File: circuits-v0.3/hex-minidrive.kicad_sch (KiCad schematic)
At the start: 97 parts, among them X1 16MHz

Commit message: Sketch out v0.3 of the servo driver, without the USB port.
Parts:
- removed D1: ~, Library:SOD-123_L2.7-W1.6-LS3.7-RD-1, symbol Library:B5819W_C8598 Schottky diode
- removed D2: ~, Library:SOT-23-3_L3.0-W1.7-P0.95-LS2.9-BR, symbol Library:PSM712-LF-T7 ETV/ESD Diodes
- removed H2: 2P-2.54mm-header, Library:HDR-TH_2P-P2.54-V-M, symbol Library:PZ254V-11-02P Connector 2P 2.54mm spacing
- removed H3: 10P 1.27mm header, Library:HDR-TH_HX-PZ1.27-1X10P-ZZ, symbol Library:HX PZ1.27-1X10P ZZ Connectors 10P 1.27mm header
- removed L3: 300mΩ, Library:L0805, symbol Library:GZ2012D601TF Ferrite bead
- removed R11, R12: 5.1kΩ, Library:R0603, symbol Library:0603WAF5101T5E Resistor 5.1kΩ
- removed USB1: ~, Library:USB-C-SMD_TYPE-C16PIN, symbol Library:TYPE-C16PIN USB connector
- renumbered FPC4 to FPC1
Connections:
- no-connect marks 21 -> 17
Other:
- note removed: "Elestrostatic discharge protection"
- note removed: "Eusebiu - USB C"
- note removed: "Ferrite bead filtering 5V USB line."
- note removed: "Note: pullup resistor is included in STM32G4 series."
- note removed: "SBU1 and SBU2 are coonected to Reset and Boot0 pins so we can flash new software over USB with the builtin bootloader, let's see if it works."
- company: (none) -> Hex Robotics Limited
- title: (none) -> Hex mini servo driver
- moved on the sheet: FPC1
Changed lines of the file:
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@@
 	(generator_version "9.0")
 	(paper "A2")
+	(title_block
+		(title "Hex mini servo driver")
+		(rev "version 0.3")
+		(company "Hex Robotics Limited")
+		(comment 1 "Author: Calin Mocanu")
+	)

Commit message: Think about v0.3 driver circuit.
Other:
- note added: "Hex Mini Driver This is a quad output, motor driver for stepper, brushless or 2 DC motors. The board comes provisioned with 2 I2C connectors for plug in rotation sensors AS5600 (preferably the Hex mini flex rotation sensor). Target limits are 6-30V supply range and 5A of current. TODO for this version: [ ] Swap components to 0402 where possible, 0603 where not. [ ] Optimize for 2 sided tiny circu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"
- note removed: "Hex Mini Driver This is a quad output, motor driver for stepper, brushless or 2 DC motors. The board comes provisioned with 2 I2C connectors for plug in rotation sensors AS5600 (preferably the Hex mini flex rotation sensor). Target limits are 6-30V supply range and 5A of current."

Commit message: Start re-wiring v0.3 motor driver, 16mm width is too tight.
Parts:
- removed C101, C201, C30, C301, C401: 1nF, Library:C0603, symbol Library:CL10B102KB8NNNC Capacitor 1nF
- removed C12, C7, C8, C803: 1uF, Library:C0603, symbol Library:CL10A105KB8NNNC Capacitor 1uF
- removed C13, C24, C25, C26, C27, C801, C802: 100nF, Library:C0603, symbol Library:CC0603KRX7R9BB104 Capacitor 100nF
- removed C20, C21: 15pF, Library:C0603, symbol Library:CL10C150JB8NNNC Capacitor 15pF
- removed C34, C9: 10nF, Library:C0603, symbol Library:0603B103K500NT Capacitor 10nF
- removed C6: 100pF, Library:C0603, symbol Library:CL10C101JB8NNNC Capacitor 100pF
- removed R10: 49.9Ω, Library:R0603, symbol Library:0603WAF499JT5E Resistor 49.9Ω
- removed R101, R102, R201, R202, R301, R302, R401, R402: 10Ω, Library:R0603, symbol Library:0603WAF100JT5E Resistor 10Ω
- removed R103, R17, R203, R303, R403, R5: 100kΩ, Library:R0603, symbol Library:0603WAF1003T5E Resistor 100kΩ
- removed R104, R204, R304, R404: 5.1kΩ, Library:R0603, symbol Library:0603WAF5101T5E Resistor 5.1kΩ
- removed R18, R801, R802: 10kΩ, Library:R0603, symbol Library:0603WAF1002T5E Resistor 10kΩ
- removed R21, R22, R23: 1.5kΩ, Library:R0603, symbol Library:0603WAF1501T5E Resistor 1.5kΩ
- removed R6: 13kΩ, Library:R0603, symbol Library:0603WAF1302T5E Resistor 13kΩ
- added C101, C106, C108, C109, C110, C111, C112, C113, C114, C21: 100nF, Library:C0402, symbol Library:CL05B104KB54PNC Capacitor 100nF 50V
- added C102, C105, C107, C31, C32: 1uF, Library:C0402, symbol Library:CL05A105KA5NQNC Capacitor 1uF
- added C103, C104: 15pF, Library:C0402, symbol Library:0402CG150J500NT Capacitor 15pF
- added C115: 1nF, Library:C0402, symbol Library:0402B102K500NT Capacitor 10nF
- added C33: 10nF, Library:C0402, symbol Library:CL05B103KB5NNNC Capacitor 10nF
- added C46: 100pF, Library:C0402, symbol Library:0402CG101J500NT Capacitor 100pF
- added R101, R102, R201, R202, R301, R302, R401, R402: 4.7Ω, Library:R0603, symbol Library:0603WAF470KT5E Resistor 4.7Ω
- added R11, R12, R13, R19: 10kΩ, Library:R0402, symbol Library:0402WGF1002TCE Resistor 10kΩ
- added R15, R16, R17: 1.5kΩ, Library:R0402, symbol Library:0402WGF1501TCE Resistor 1.5kΩ
- added R18, R42: 100kΩ, Library:R0402, symbol Library:0402WGF1003TCE Resistor 100kΩ
- added R41: 49.9Ω, Library:R0402, symbol Library:0402WGF499JTCE Resistor 49.9Ω
- added R43: 13.3kΩ, Library:R0402, symbol Library:FRC0402F1332TS Resistor 13.3kΩ
- renumbered C10 to C0, C11 to C1, C14 to C2, C15 to C3, C16 to C4, C3 to C41, C2 to C42, C1 to C43, C4 to C44, C5 to C45, C17 to C5, C18 to C6, U8 to U2
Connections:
- net 3V3: now also C109.2, C111.2, C112.2, C113.2, C21.2, C32.2
- net 3V3A: now also C101.2, C102.2
- net 5V: now also C31.2, R41.2
- net ADC2_IN15/VOLTAGE: now also C115.2, R18.1, R19.2
- net BOOT0/STOP: now also C114.2, R11.2
- net Blue-LED: now also R16.1
- net Buck-FB: now also C46.1, R42.1, R43.2
- net Buck-Probe-Point: now also C46.2, R41.1, R42.2
- net GND: now also C101.1, C102.1, C103.1, C104.1, C105.1, C106.1, C107.1, C108.1, C109.1, C110.1, C111.1, C112.1, C113.1, C114.1, C115.1, C21.1, C31.1, C32.1, C33.1, R11.1, R12.1, R19.1, R43.1
- net Gate-1-Negative: now also R101.2
- net Gate-1-Positive: now also R102.1
- net Gate-2-Negative: now also R201.2
- net Gate-2-Positive: now also R202.1
- net Gate-3-Negative: now also R301.2
- net Gate-3-Positive: now also R302.1
- net Gate-4-Negative: now also R401.2
- net Gate-4-Positive: now also R402.1
- net Green-LED: now also R15.1
- net LDO-Bypass-Capacitor: now also C33.2
- net N-Gate-1: now also R101.1
- net N-Gate-2: now also R201.1
- net N-Gate-3: now also R301.1
- net N-Gate-4: now also R401.1
- net NRST: now also C110.2
- net OSC1: now also C103.2
- net OSC2: now also C104.2
- net P-Gate-1: now also R102.2
- net P-Gate-2: now also R202.2
- net P-Gate-3: now also R302.2
- net P-Gate-4: now also R402.2
- net Red-LED: now also R17.2
- net SYS_JTCK-SWCLK: now also FPC2.6, FPC3.6
- net SYS_JTMS-SVDIO: now also FPC2.5, FPC3.5
- net TIM2_CH3/BLUE_LED: now also R16.2
- net TIM4_CH1/RED_LED: now also R17.1
- net TIM4_CH2/GREEN_LED: now also R15.2
- net VCC: now also R18.2
- net VREF: now reaches U1.28 (VREF+)
- net VREF: now also C105.2, C106.2, R13.2
- net ADC1_IN11/M4_VOLTAGE: no longer names the net of U1.34 (PB12)
- net ADC1_IN3/HALF_3V3_REF renamed ADC1_IN3/HALF_VREF
- net ADC1_IN3/HALF_VREF: now also C107.2, C108.2, R12.2, R13.1; no longer U1.17 (PA3), U1.19 (PA5), U1.26 (PB2)
- net ADC1_IN7/POT_1: no longer names the net of U1.9 (PC1)
- net ADC1_IN8/POT_2: no longer names the net of U1.10 (PC2)
- net ADC2_IN17/POT_3: no longer names the net of U1.18 (PA4)
- net DIRECTION_SWITCH: no longer names the net of U1.55 (PD2)
- removed net FREE_IO_1: FPC2.5, FPC3.5, U1.3 (PC14-OSC32_IN)
- removed net FREE_IO_2: FPC2.6, FPC3.6, U1.4 (PC15-OSC32_OUT)
- net OPAMP1_VINP/M1_VOLTAGE: no longer names the net of U1.13 (PA1)
- net OPAMP2_VINP/M2_VOLTAGE: no longer names the net of U1.21 (PA7)
- net OPAMP3_VINP/M3_VOLTAGE: no longer names the net of U1.35 (PB13)
- net TOOL_SWITCH: no longer names the net of U1.58 (PB5)
- net USB_D_N: no longer names the net of U1.45 (PA11)
- net USB_D_P: no longer names the net of U1.46 (PA12)
- no-connect marks 17 -> 32
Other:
- note added: "Hex Mini Driver This is a quad output, motor driver for stepper, brushless or 2 DC motors. The board comes provisioned with 2 I2C connectors for plug in rotation sensors AS5600 (preferably the Hex mini flex rotation sensor). Target limits are 6-30V supply range and 5A of current. TODO for this version: [v] Swap components to 0402 where possible, 0603 where not. [v] Optimize for 2 sided tiny circu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"
- note added: "We absolutely need this resistor even if we don't use the 5V LDO."
- note removed: "Can this resistor be removed and the pin left unconnected?"
- note removed: "Debug connector"
- note removed: "Hex Mini Driver This is a quad output, motor driver for stepper, brushless or 2 DC motors. The board comes provisioned with 2 I2C connectors for plug in rotation sensors AS5600 (preferably the Hex mini flex rotation sensor). Target limits are 6-30V supply range and 5A of current. TODO for this version: [ ] Swap components to 0402 where possible, 0603 where not. [ ] Optimize for 2 sided tiny circu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"
- note removed: "This motor voltage is not amplified as we only need 2 voltage probes for stepper motors. However, we need the bridge voltage to verify if the mosfets were on during the driving phase."
- note removed: "This small resistor is for testing purposes (so says the datasheet)."
- note removed: "Use a bigger division ratio for the motor voltage because we will bias it to half VDA to measure both positive and negative EMF."
- moved on the sheet: C501, C601, L2, LED1, R501, R601, U1, U2, U5, U6, X1

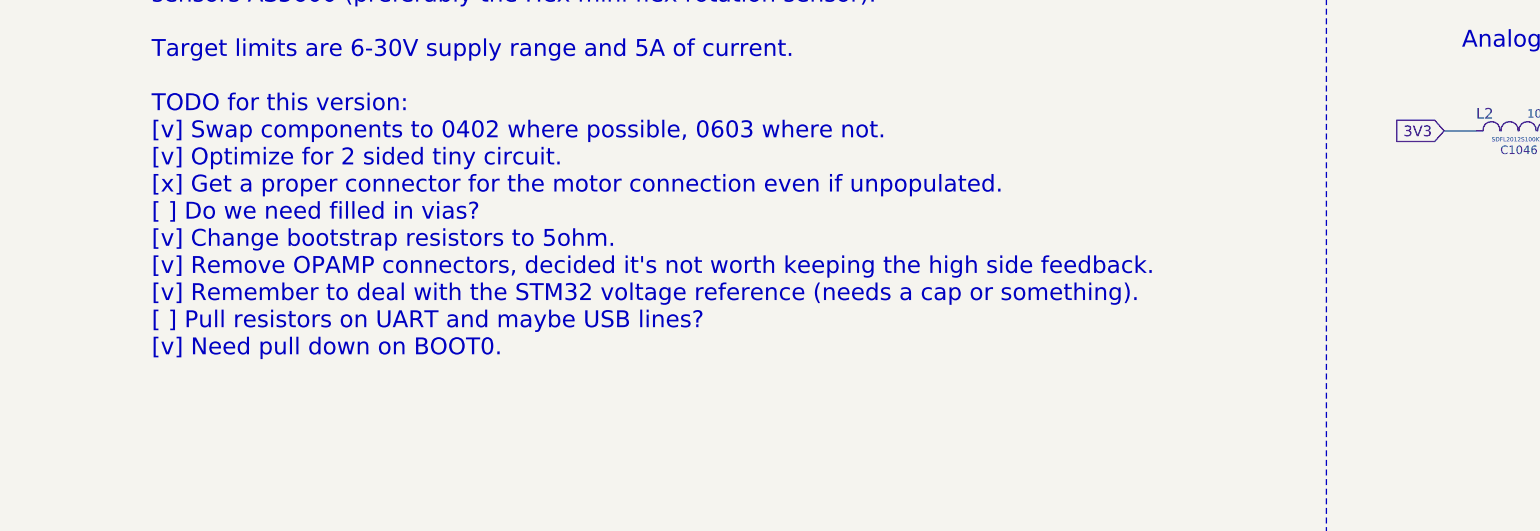
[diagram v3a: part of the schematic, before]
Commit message: Finished v0.3 circuit layout.
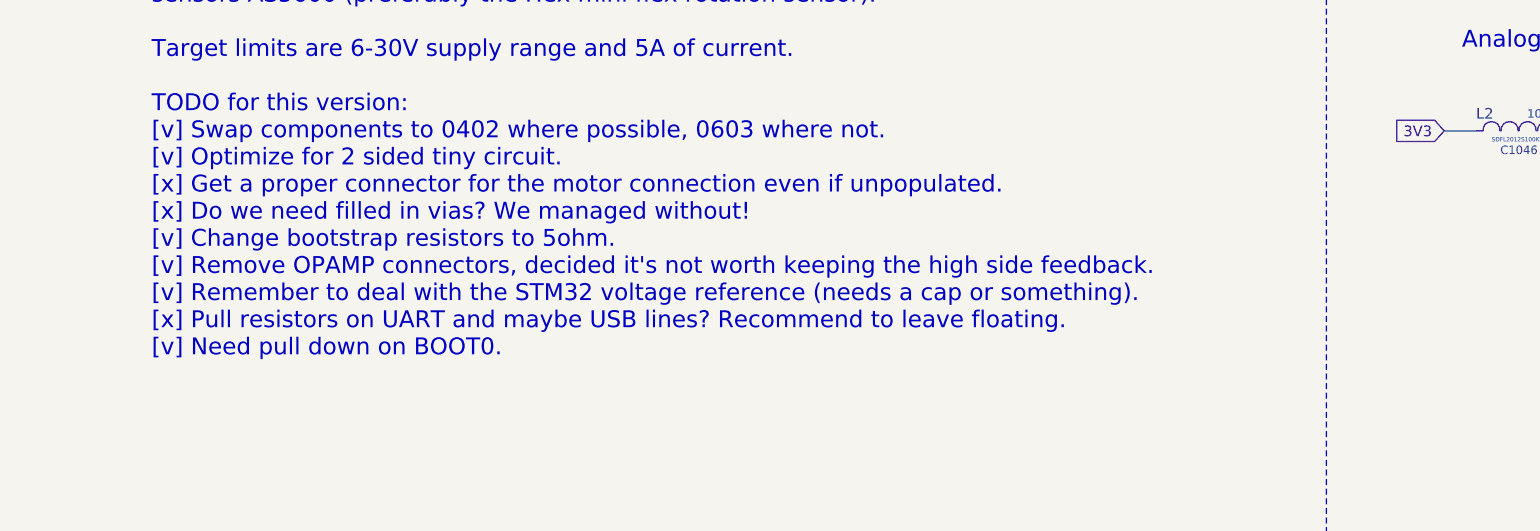
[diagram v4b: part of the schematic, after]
